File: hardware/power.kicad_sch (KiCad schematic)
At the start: 34 parts, among them U3 TI LMR51430YFDDCR, U4 TI LMR51430YFDDCR, U5 TPS2116DRLR, U6 NCV8187AMT180TAG, U7 LP5912-3.3DRVR

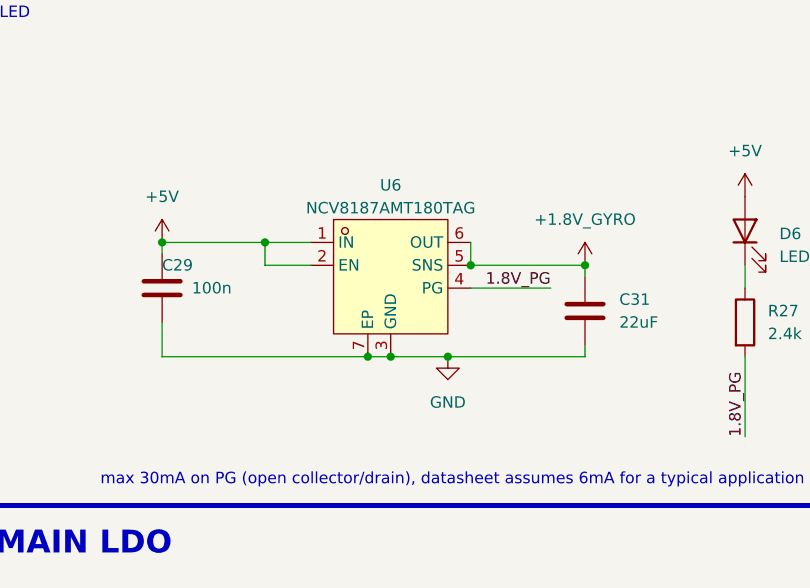
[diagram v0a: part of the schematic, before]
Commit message: hardware: add LP5912-1.8 LDO (U15) and layout working state
- New LP5912-1.8DRVR symbol in project lib, WSON-6 2x2mm footprint with
  thermal vias, matching STEP model
- LP5912-1.8 added to power sheet as U15
- OpenFC.kicad_pcb layout working state carrying the change
- .kicad_pro used_designators updated (U15)

Co-Authored-By: Claude Fable 5 <noreply@anthropic.com>
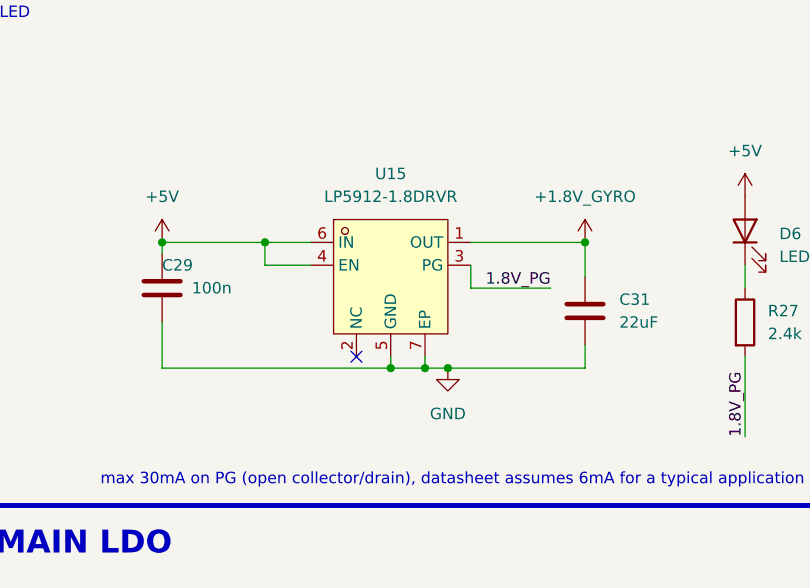
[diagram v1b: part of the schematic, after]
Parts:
- removed U6: NCV8187AMT180TAG, lib:WDFN-6_L2.0-W2.0-P0.65-BL-EP, symbol lib:NCV8187AMT180TAG
- added U15: LP5912-1.8DRVR, lib:WSON-6_L2.0-W2.0-P0.65-TL-EP, symbol lib:LP5912-1.8DRVR
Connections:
- net +1.8V_GYRO: now also U15.1 (OUT)
- net +5V: now also U15.4 (EN), U15.6 (IN)
- net 1.8V_PG: now also U15.3 (PG)
- net GND: now also U15.5 (GND), U15.7 (EP)
- no-connect marks 1 -> 2

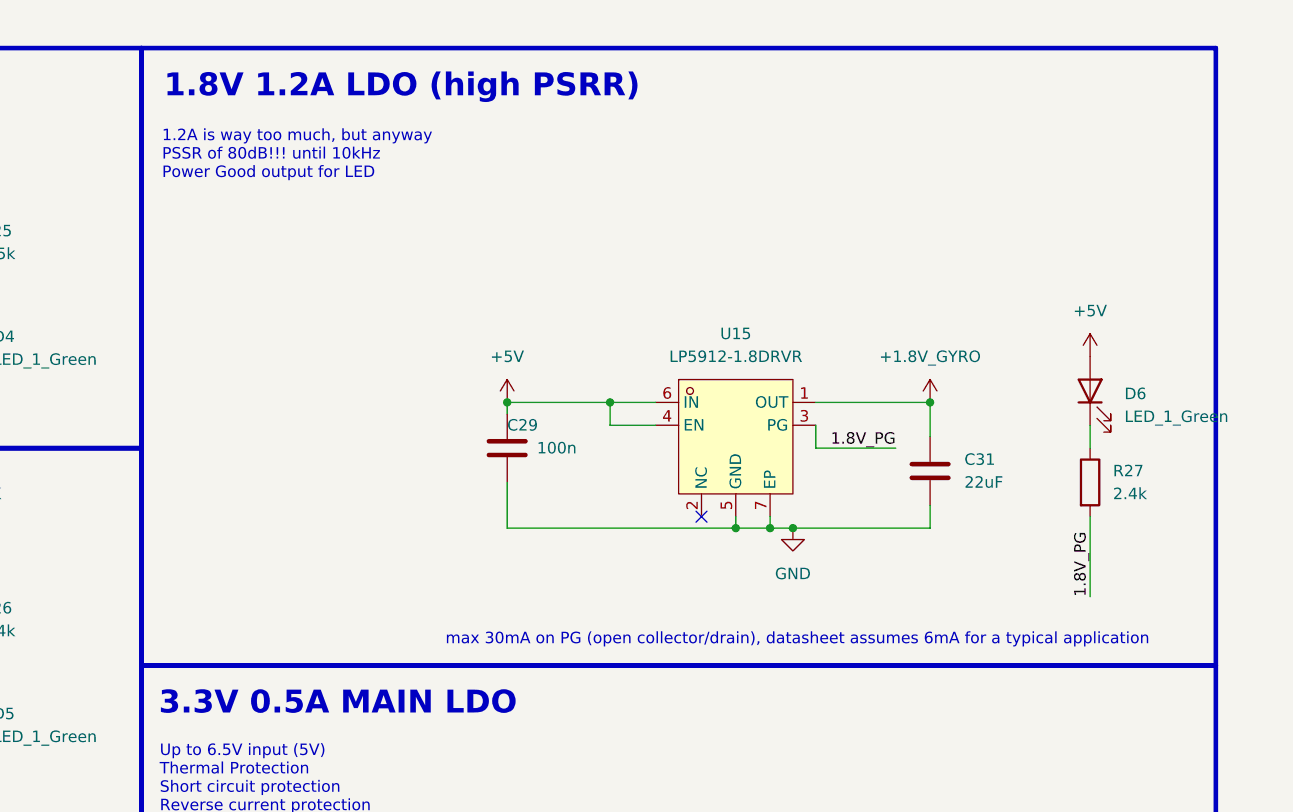
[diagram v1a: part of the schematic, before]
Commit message: Swap 1.8V LDO and IMU, fix BOM/CPL export hygiene
Mirrors the same pass done on OpenFC-Lite-Mini.

Part changes:
- NCV8187AMT180TAG (stock 0 at JLC) replaced by U15 LP5912-1.8DRVR
  (C2876234), same WSON-6 2x2 land pattern as the LP5912-3.3, PG retained.
- U9 LSM6DSV16XTR replaced by BMI270 (C2836813) in the schematic. Bosch
  Table 22 matches the existing LGA-14 symbol pin for pin, so no rewire.

Export fixes:
- U15, CN1 and U13 carried their part numbers in a field named "LCSC Part"
  rather than "LCSC" and exported blank. Renamed. CN1 (C160404) and U13
  (C160403) are real JST connectors and stay in the BOM.
- J3, J6, J10, J16, J19, J23 (lib:small_pad) and TP1 to TP4 (TestPoint) were
  still reaching the BOM with no part number. Set to in_bom=no, on_board=yes,
  dnp=no: copper stays, BOM entry goes.
- 57 pad and testpoint footprints now carry exclude_from_bom plus
  exclude_from_pos_files instead of the dnp flag. Previously 47 pads leaked
  into the position file on every export.

BOM and CPL now agree at 111 placements with no blank part numbers, exported
without any dnp flag. ERC is unchanged against HEAD (198 vs 199 violations,
all pre-existing).

Known outstanding, not in this commit: C32 is still C105226 while C42 is
C415703, and the PCB copy of U9 still carries the LSM6 part number until
Update PCB from Schematic is run. The panel file is deleted in the working
tree pending a rebuild and is deliberately left uncommitted.

Co-Authored-By: Claude Fable 5 <noreply@anthropic.com>
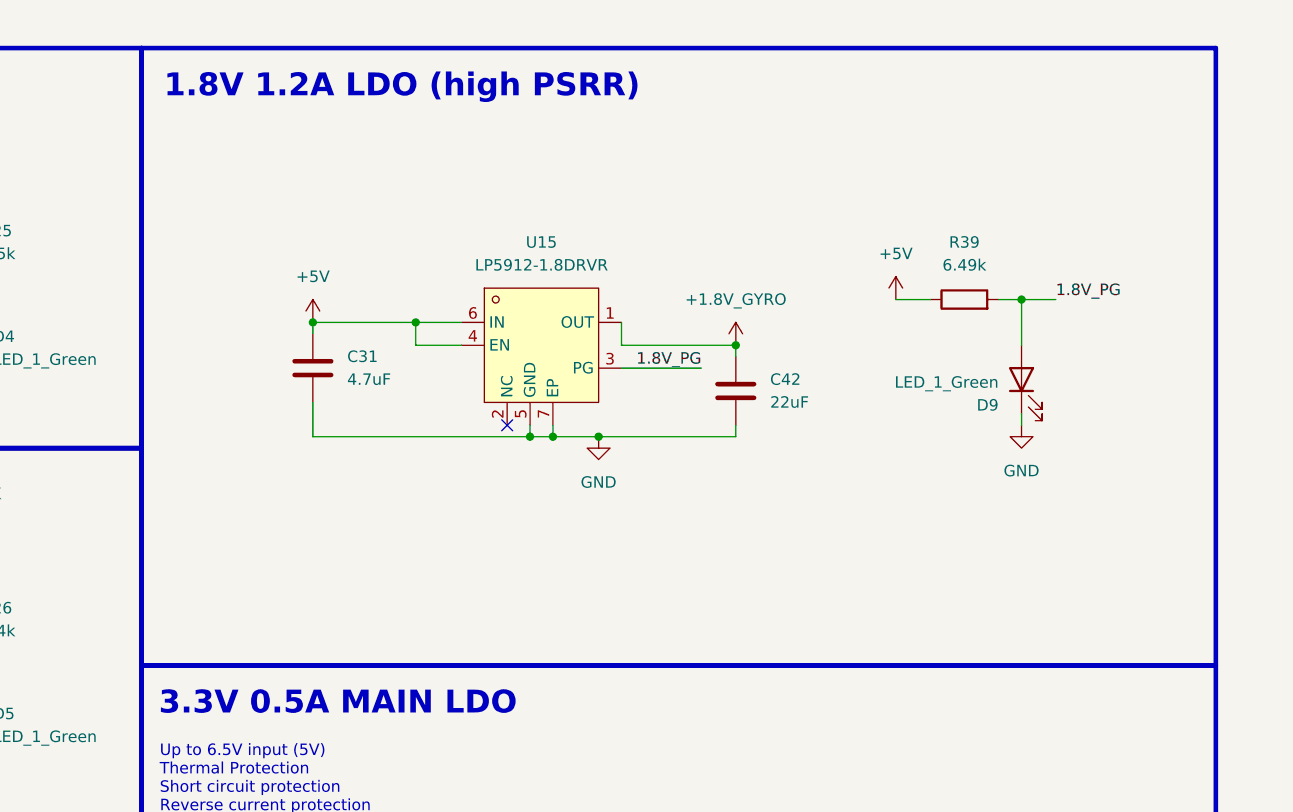
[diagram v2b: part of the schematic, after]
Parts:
- removed C29: 100n, Capacitor_SMD:C_0201_0603Metric, symbol Device:C
- removed D6: LED_1_Green, LED_SMD:LED_0402_1005Metric, symbol Device:LED
- removed R27: 2.4k, Resistor_SMD:R_0201_0603Metric, symbol Device:R
- added C42: 22uF, Capacitor_SMD:C_0402_1005Metric, symbol Device:C
- added D9: LED_1_Green, LED_SMD:LED_0402_1005Metric, symbol Device:LED
- added R39: 6.49k, Resistor_SMD:R_0201_0603Metric, symbol Device:R
- C31: value 22uF -> 4.7uF; LCSC C105226 -> C23733; MPN CL05A226MQ5QUNC -> CL05A475MP5NRNC
- U15: footprint lib:WSON-6_L2.0-W2.0-P0.65-TL-EP -> lib:WSON-6-1EP_2x2mm_P0.65mm_EP1x1.6mm_ThermalVias; LCSC (none) -> C2876234; LCSC Part C2876234 -> (none)
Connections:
- net +1.8V_GYRO: now also C42.1; no longer C31.1
- net +5V: now also C31.1, R39.1
- net 1.8V_PG: now also D9.2 (A), R39.2
- net GND: now also C42.2, D9.1 (K)
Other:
- note removed: "1.2A is way too much, but anyway PSSR of 80dB!!! until 10kHz Power Good output for LED"
- note removed: "max 30mA on PG (open collector/drain), datasheet assumes 6mA for a typical application"

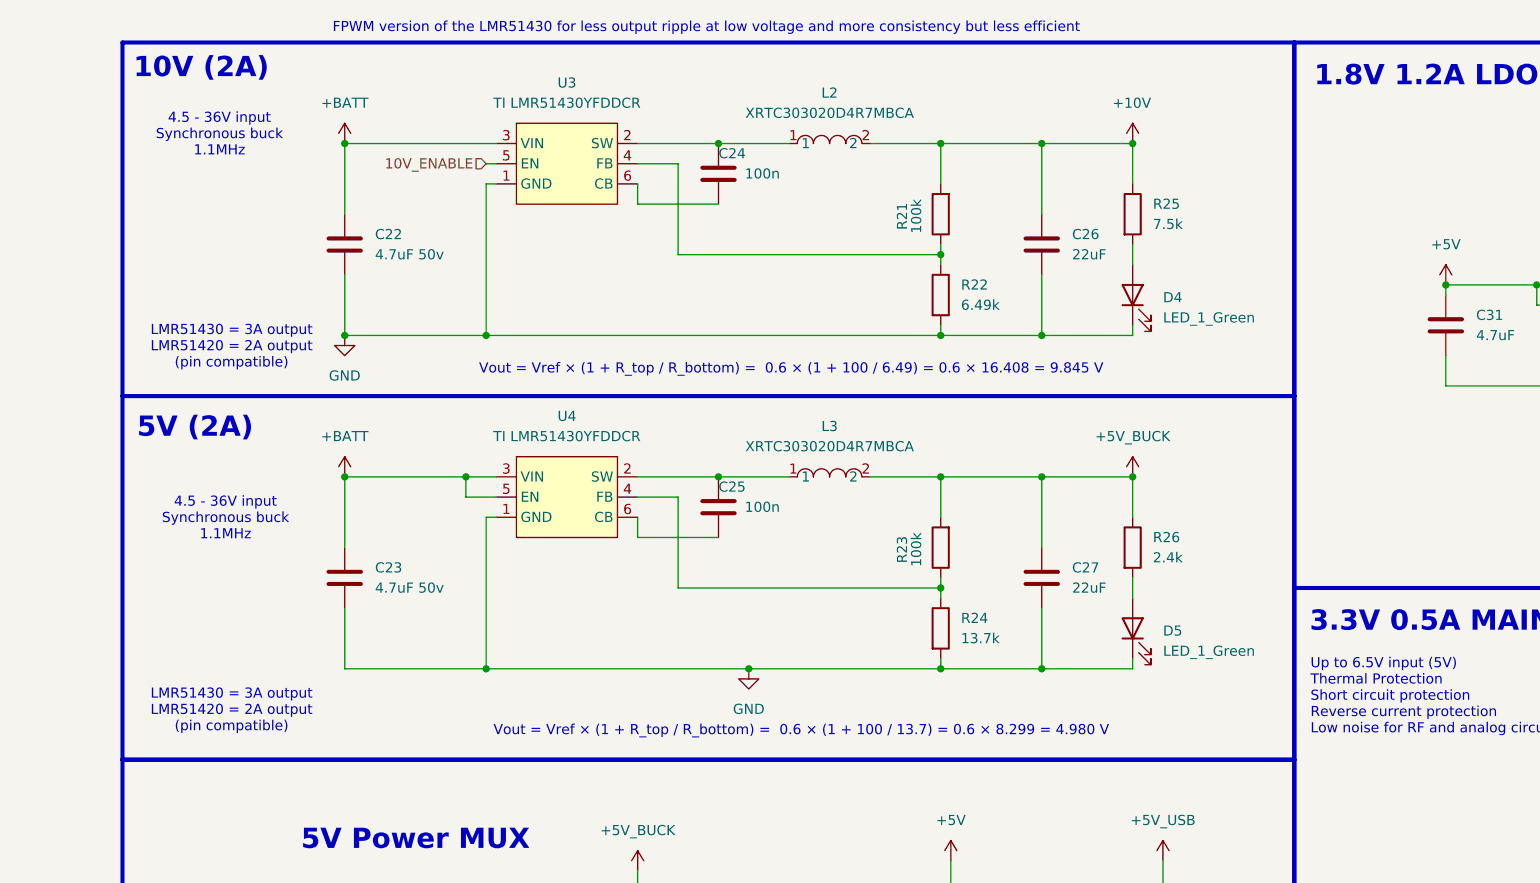
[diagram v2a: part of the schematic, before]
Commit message: Rev 3: 8S bucks, LP5912 gyro LDO, BMI270, drop the panel project
Power: both bucks are LMR51635YDDCR (U6, U16, C45262770), 4.3-60 V with a 63 V
absolute maximum, replacing the LMR51430YFDDCR whose 38 V absolute maximum left
no margin at 8S. The reference moves from 0.6 V to 0.8 V so the feedback
dividers follow: R22 8.87k for 9.82 V and R24 19.1k for 4.99 V. Same SOT-23-6
land pattern, different pinout, so both buck corners are re-routed.

Gyro supply: U15 LP5912-1.8DRVR placed, along with D9 and R39 which existed in
the Rev 2 schematic but were never placed in the Rev 2 layout. The unused
NCV8187AMT180TAG footprint is gone.

IMU: BMI270 (U9).

Panel: OpenFC_Panel.kicad_pcb and .kicad_pro removed. Production sets come from
OpenFC.kicad_pcb directly now; README updated to match.

ERC and DRC reviewed by the maintainer.

Co-Authored-By: Claude Opus 5 (1M context) <noreply@anthropic.com>
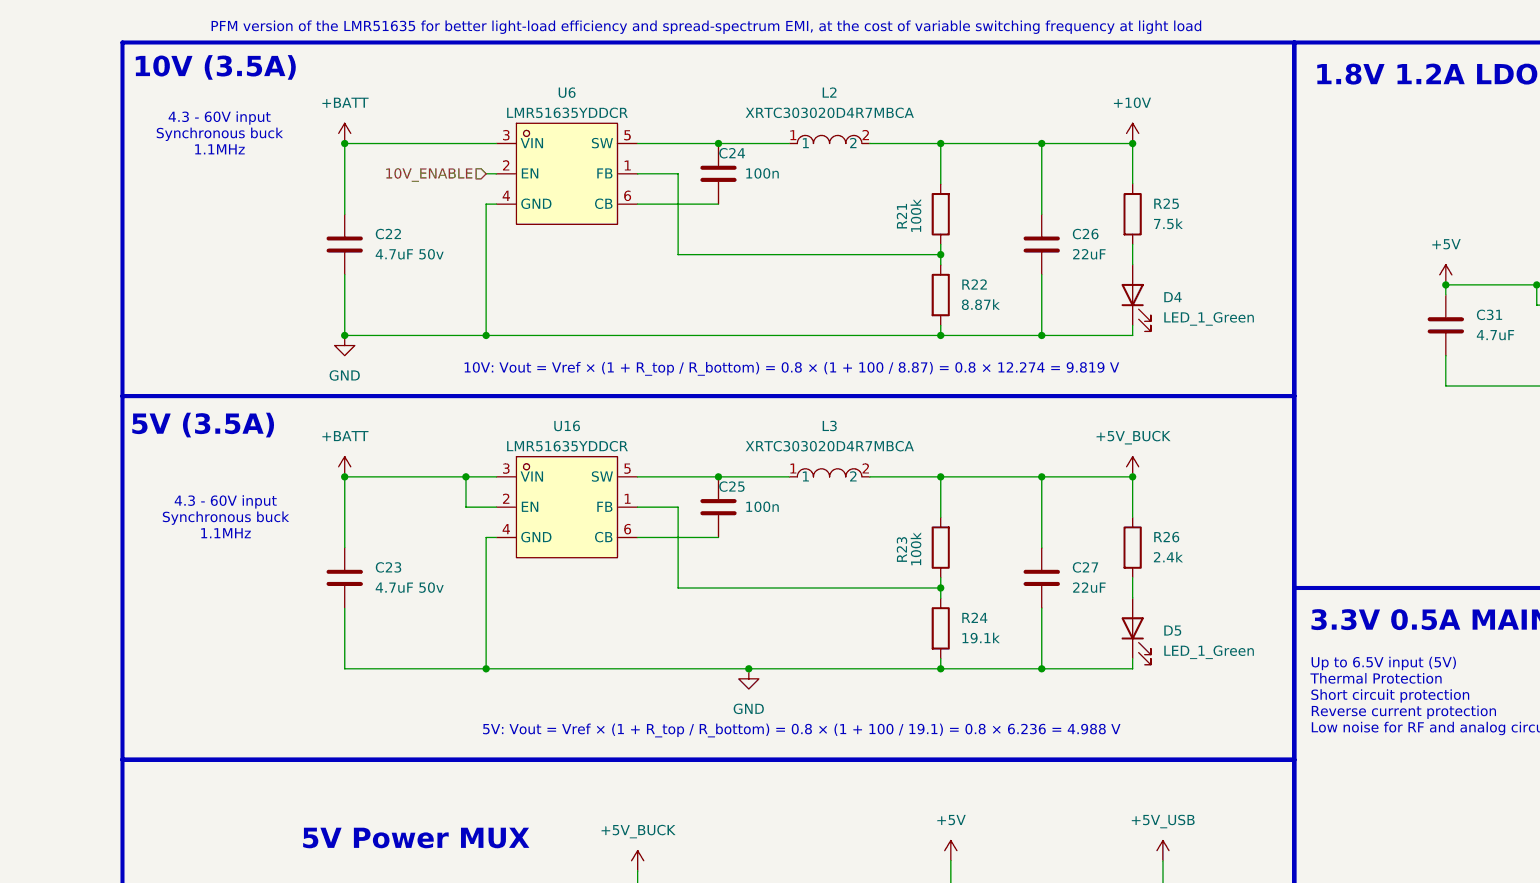
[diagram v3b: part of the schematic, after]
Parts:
- removed U3, U4: TI LMR51430YFDDCR, lib:SOT-23-6_L2.9-W1.6-P0.95-LS2.9-BL, symbol lib:LMR51420YDDCR
- added U16, U6: LMR51635YDDCR, lib:SOT-23-6_L2.9-W1.6-P0.95-LS2.8-BL, symbol lib:LMR51635YDDCR
- R22: value 6.49k -> 8.87k; LCSC C2107920 -> C332577
- R24: value 13.7k -> 19.1k; LCSC C320695 -> C320741; MPN RC-01W1372FT -> RC-01W1912FT
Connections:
- net +BATT: now also U16.2 (EN), U16.3 (VIN), U6.3 (VIN)
- net 10V_ENABLE: now also U6.2 (EN)
- net GND: now also U16.4 (GND), U6.4 (GND)
- net at R21.1, R22.1: now also U6.1 (FB)
- net at R23.1, R24.1: now also U16.1 (FB)
- net at C24.1, L2.1: now also U6.5 (SW)
- net at C24.2: now also U6.6 (CB)
- net at C25.1, L3.1: now also U16.5 (SW)
- net at C25.2: now also U16.6 (CB)
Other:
- note added: "10V (3.5A)"
- note added: "10V: Vout = Vref × (1 + R_top / R_bottom) = 0.8 × (1 + 100 / 8.87) = 0.8 × 12.274 = 9.819 V"
- note added: "4.3 - 60V input Synchronous buck 1.1MHz"
- note added: "5V (3.5A)"
- note added: "5V: Vout = Vref × (1 + R_top / R_bottom) = 0.8 × (1 + 100 / 19.1) = 0.8 × 6.236 = 4.988 V"
- note added: "PFM version of the LMR51635 for better light-load efficiency and spread-spectrum EMI, at the cost of variable switching frequency at light load"
- note removed: "10V (2A)"
- note removed: "4.5 - 36V input Synchronous buck 1.1MHz"
- note removed: "5V (2A)"
- note removed: "FPWM version of the LMR51430 for less output ripple at low voltage and more consistency but less efficient"
- note removed: "LMR51430 = 3A output LMR51420 = 2A output (pin compatible)"
- note removed: "Vout = Vref × (1 + R_top / R_bottom) = 0.6 × (1 + 100 / 13.7) = 0.6 × 8.299 = 4.980 V"
- note removed: "Vout = Vref × (1 + R_top / R_bottom) = 0.6 × (1 + 100 / 6.49) = 0.6 × 16.408 = 9.845 V"

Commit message: 4V5 rework: TPS2116 mux replaced by DSK24 diode-OR
U5, its RB161QS diodes, R19/R20 and C28 removed. D6 from the buck
output and D10 from +5V_USB feed the new +4v5 net, which supplies the
3.3 V and 1.8 V LDOs, the 6-pin JST and the J5/J47 pads. The buck
output is plain +5V and drives the external 5 V pads directly. All 596
vias at 0.35/0.2, so the line-standard floors pass. DSK24 footprint and
3D model committed with the change. DRC severity choices per Stan.

Co-Authored-By: Claude Opus 5 (1M context) <noreply@anthropic.com>
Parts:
- removed C28: 4.7uF, Capacitor_SMD:C_0402_1005Metric, symbol Device:C
- removed D2, D3: RB161QS-40_C28646385, lib:SOD-882_L1.0-W0.6-RD, symbol lib:RB161QS-40_C28646385
- removed R19: 100k, Resistor_SMD:R_0201_0603Metric, symbol Device:R
- removed R20: 39k, Resistor_SMD:R_0201_0603Metric, symbol Device:R
- removed U5: TPS2116DRLR, lib:SOT-583-8_L2.1-W1.6-P0.50-LS1.6-BL, symbol lib:TPS2116DRLR
- added D10, D6: DSK24, lib:SOD-123_L2.8-W1.8-LS3.7-RD, symbol lib:DSK24_C64890
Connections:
- net +5V_BUCK is gone; now on net +5V: C27.1, L3.2, R23.2, R26.1
- net +5V: now also D6.2 (A); no longer C30.1, C31.1, R39.1, U15.4 (EN), U15.6 (IN), U7.4 (EN), U7.6 (IN)
- net +5V_USB: now also D10.2 (A)
- new net +4v5: C30.1, C31.1, D10.1 (K), D6.1 (K), R39.1, U15.4 (EN), U15.6 (IN), U7.4 (EN), U7.6 (IN)
- no-connect marks 2 -> 1

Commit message: schematics: complete Manufacturer/MPN coverage, trim stray whitespace
16 field fixes: Manufacturer backfilled from the LCSC catalogue on osd,
power and rp2350a sheets, trailing space trimmed from four XL-1005UGC MPNs.
Part of the fab-agnostic BOM standardisation for quoting outside JLCPCB.

kicad-skip reflowed the touched files; structural diff against the originals
shows only property changes, ERC identical (179 violations before and after).

Co-Authored-By: Claude Fable 5 <noreply@anthropic.com>
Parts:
- D4, D5, D7, D9: MPN XL-1005UGC -> XL-1005UGC
- R22: MPN (none) -> RTT018871FTH; Manufacturer (none) -> RALEC
- R25: MPN (none) -> RC0201FR-077K5L; Manufacturer (none) -> YAGEO
- R26: MPN (none) -> RTT012401FTH; Manufacturer (none) -> RALEC
- R28: MPN (none) -> RC0201FR-07510RL; Manufacturer (none) -> YAGEO
- R39: MPN (none) -> AF0201FR-076K49L; Manufacturer (none) -> YAGEO
